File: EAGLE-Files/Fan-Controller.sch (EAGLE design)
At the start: 5 parts, among them T1 BC337

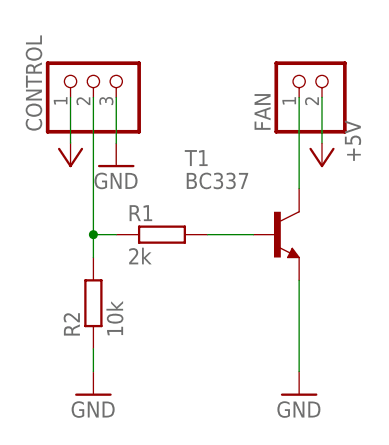
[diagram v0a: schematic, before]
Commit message: Updated all boards for JLCPCB order
Also added the controller boards and schematics back
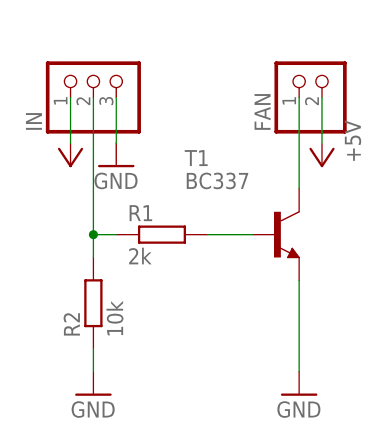
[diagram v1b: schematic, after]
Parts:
- renumbered CONTROL to IN
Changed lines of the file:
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@@
 <part name="GND3" library="supply1" library_urn="urn:adsk.eagle:library:371" deviceset="GND" device=""/>
 <part name="FAN" library="pinhead" library_urn="urn:adsk.eagle:library:325" deviceset="PINHD-1X2" device="/90" package3d_urn="urn:adsk.eagle:package:22437/2"/>
-<part name="CONTROL" library="pinhead" library_urn="urn:adsk.eagle:library:325" deviceset="PINHD-1X3" device="/90" package3d_urn="urn:adsk.eagle:package:22459/2"/>
+<part name="IN" library="pinhead" library_urn="urn:adsk.eagle:library:325" deviceset="PINHD-1X3" device="/90" package3d_urn="urn:adsk.eagle:package:22459/2"/>
 <part name="GND4" library="supply1" library_urn="urn:adsk.eagle:library:371" deviceset="GND" device=""/>
 <part name="P+3" library="supply1" library_urn="urn:adsk.eagle:library:371" deviceset="+5V" device=""/>
@@
 <attribute name="VALUE" x="68.58" y="39.37" size="1.778" layer="96" rot="R90"/>
 </instance>
-<instance part="CONTROL" gate="A" x="38.1" y="45.72" smashed="yes" rot="R90">
+<instance part="IN" gate="A" x="38.1" y="45.72" smashed="yes" rot="R90">
 <attribute name="NAME" x="32.385" y="39.37" size="1.778" layer="95" rot="R90"/>
 <attribute name="VALUE" x="45.72" y="39.37" size="1.778" layer="96" rot="R90"/>
@@
 </segment>
 <segment>
-<pinref part="CONTROL" gate="A" pin="3"/>
+<pinref part="IN" gate="A" pin="3"/>
 <pinref part="GND4" gate="1" pin="GND"/>
 <wire x1="40.64" y1="43.18" x2="40.64" y2="38.1" width="0.1524" layer="91"/>
@@
 <segment>
 <pinref part="P+3" gate="1" pin="+5V"/>
-<pinref part="CONTROL" gate="A" pin="1"/>
+<pinref part="IN" gate="A" pin="1"/>
 <wire x1="35.56" y1="38.1" x2="35.56" y2="43.18" width="0.1524" layer="91"/>
 </segment>
@@
 <wire x1="38.1" y1="25.4" x2="38.1" y2="27.94" width="0.1524" layer="91"/>
 <junction x="38.1" y="27.94"/>
-<pinref part="CONTROL" gate="A" pin="2"/>
+<pinref part="IN" gate="A" pin="2"/>
 <wire x1="38.1" y1="43.18" x2="38.1" y2="27.94" width="0.1524" layer="91"/>
 </segment>
